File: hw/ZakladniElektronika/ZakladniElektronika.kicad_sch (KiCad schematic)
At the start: 2 parts, among them J10 Conn_01x40, J11 Conn_01x40

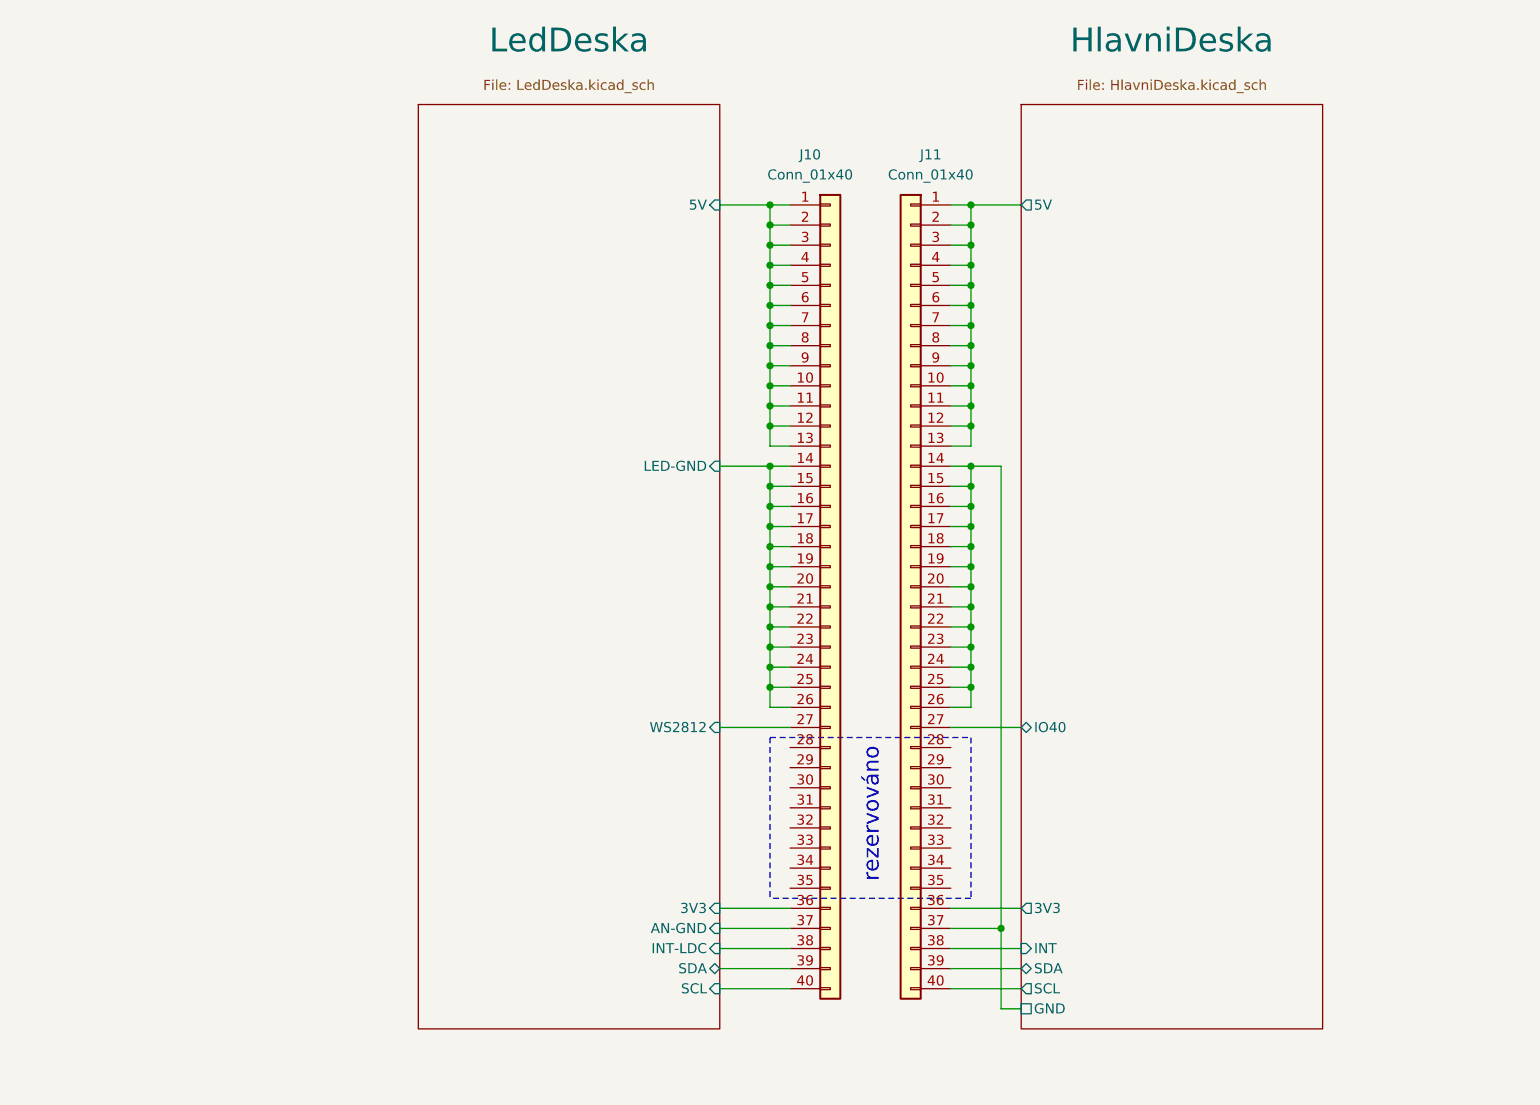
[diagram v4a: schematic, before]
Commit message: Výmněna ochrany baterie
Předchozí ochranný čip JLCPCB nemělo na skladě
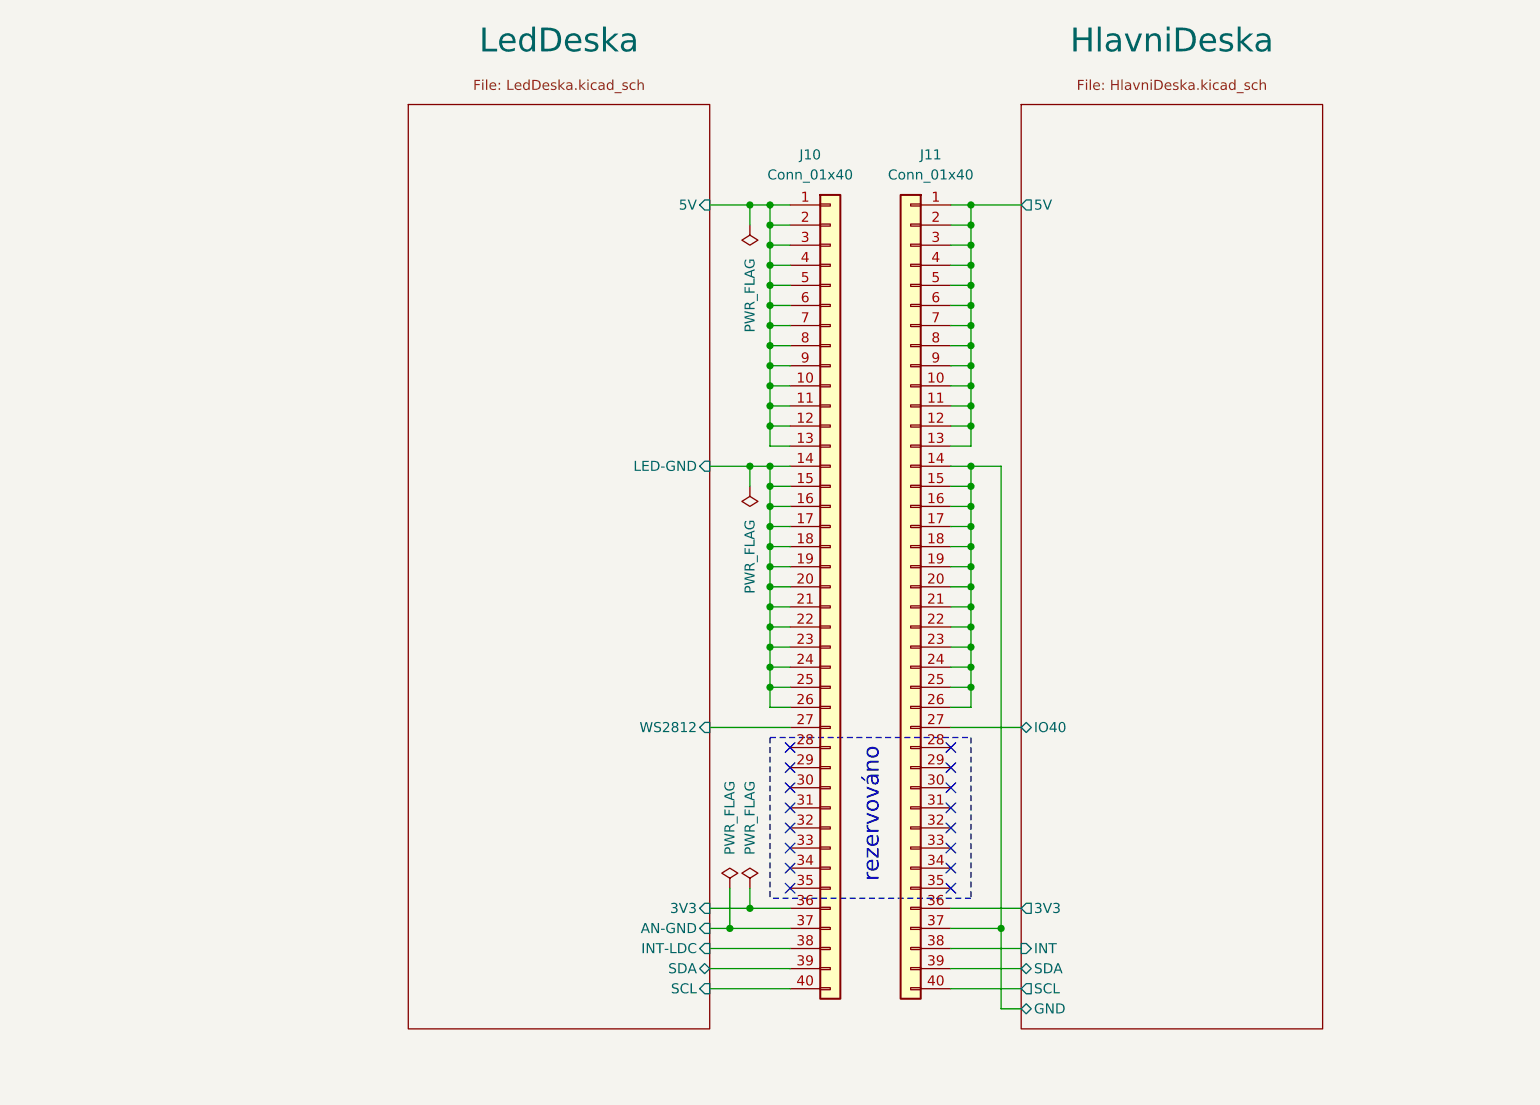
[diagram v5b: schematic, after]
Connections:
- no-connect marks 0 -> 16
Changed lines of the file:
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@@
   (junction (at 146.05 48.26) (diameter 0) (color 0 0 0 0)
   )
+  (junction (at 143.51 134.62) (diameter 0) (color 0 0 0 0)
+  )
   (junction (at 146.05 86.36) (diameter 0) (color 0 0 0 0)
   )
+  (junction (at 140.97 137.16) (diameter 0) (color 0 0 0 0)
+  )
   (junction (at 146.05 106.68) (diameter 0) (color 0 0 0 0)
   )
@@
   (junction (at 146.05 53.34) (diameter 0) (color 0 0 0 0)
   )
+  (junction (at 143.51 45.72) (diameter 0) (color 0 0 0 0)
+  )
   (junction (at 146.05 73.66) (diameter 0) (color 0 0 0 0)
   )
@@
   (junction (at 171.45 71.12) (diameter 0) (color 0 0 0 0)
   )
+  (junction (at 143.51 78.74) (diameter 0) (color 0 0 0 0)
+  )
   (junction (at 146.05 55.88) (diameter 0) (color 0 0 0 0)
   )
@@
   (junction (at 171.45 73.66) (diameter 0) (color 0 0 0 0)
   )
+  (no_connect (at 148.59 127))
+  (no_connect (at 148.59 129.54))
+  (no_connect (at 148.59 116.84))
+  (no_connect (at 168.91 127))
+  (no_connect (at 148.59 119.38))
+  (no_connect (at 148.59 132.08))
+  (no_connect (at 168.91 121.92))
+  (no_connect (at 168.91 116.84))
+  (no_connect (at 168.91 114.3))
+  (no_connect (at 168.91 124.46))
+  (no_connect (at 168.91 132.08))
+  (no_connect (at 168.91 119.38))
+  (no_connect (at 148.59 114.3))
+  (no_connect (at 148.59 121.92))
+  (no_connect (at 148.59 124.46))
+  (no_connect (at 168.91 129.54))
   (wire (pts (xy 177.8 45.72) (xy 171.45 45.72))
     (stroke (width 0) (type default))
@@
     (stroke (width 0) (type default) (color 0 0 0 1))
   )
-  (wire (pts (xy 139.7 134.62) (xy 148.59 134.62))
+  (wire (pts (xy 138.43 134.62) (xy 143.51 134.62))
     (stroke (width 0) (type default))
   )
@@
     (stroke (width 0) (type default) (color 0 0 0 1))
   )
-  (wire (pts (xy 139.7 144.78) (xy 148.59 144.78))
+  (wire (pts (xy 138.43 144.78) (xy 148.59 144.78))
     (stroke (width 0) (type default))
   )
@@
     (stroke (width 0) (type default))
   )
+  (wire (pts (xy 143.51 81.28) (xy 143.51 78.74))
+    (stroke (width 0) (type default))
+  )
   (wire (pts (xy 168.91 142.24) (xy 177.8 142.24))
     (stroke (width 0) (type default))
@@
     (stroke (width 0) (type default))
   )
+  (wire (pts (xy 143.51 45.72) (xy 146.05 45.72))
+    (stroke (width 0) (type default))
+  )
   (wire (pts (xy 168.91 50.8) (xy 171.45 50.8))
     (stroke (width 0) (type default))
@@
     (stroke (width 0) (type default))
   )
+  (wire (pts (xy 143.51 134.62) (xy 148.59 134.62))
+    (stroke (width 0) (type default))
+  )
   (wire (pts (xy 148.59 60.96) (xy 146.05 60.96))
     (stroke (width 0) (type default))
@@
     (stroke (width 0) (type default))
   )
-  (wire (pts (xy 139.7 142.24) (xy 148.59 142.24))
+  (wire (pts (xy 138.43 142.24) (xy 148.59 142.24))
     (stroke (width 0) (type default))
   )
@@
   )
   (wire (pts (xy 148.59 99.06) (xy 146.05 99.06))
+    (stroke (width 0) (type default))
+  )
+  (wire (pts (xy 140.97 132.08) (xy 140.97 137.16))
     (stroke (width 0) (type default))
   )
@@
     (stroke (width 0) (type default))
   )
-  (wire (pts (xy 139.7 137.16) (xy 148.59 137.16))
+  (wire (pts (xy 138.43 137.16) (xy 140.97 137.16))
     (stroke (width 0) (type default))
   )
@@
     (stroke (width 0) (type default))
   )
-  (wire (pts (xy 139.7 111.76) (xy 148.59 111.76))
+  (wire (pts (xy 138.43 111.76) (xy 148.59 111.76))
     (stroke (width 0) (type default))
   )
@@
     (stroke (width 0) (type default) (color 0 0 0 1))
   )
+  (wire (pts (xy 143.51 78.74) (xy 146.05 78.74))
+    (stroke (width 0) (type default))
+  )
   (wire (pts (xy 171.45 86.36) (xy 171.45 83.82))
     (stroke (width 0) (type default) (color 0 0 0 1))
@@
     (stroke (width 0) (type default))
   )
+  (wire (pts (xy 143.51 48.26) (xy 143.51 45.72))
+    (stroke (width 0) (type default))
+  )
   (wire (pts (xy 168.91 83.82) (xy 171.45 83.82))
     (stroke (width 0) (type default) (color 0 0 0 1))
   )
-  (wire (pts (xy 139.7 78.74) (xy 146.05 78.74))
+  (wire (pts (xy 138.43 78.74) (xy 143.51 78.74))
     (stroke (width 0) (type default))
   )
@@
     (stroke (width 0) (type default))
   )
-  (wire (pts (xy 139.7 45.72) (xy 146.05 45.72))
+  (wire (pts (xy 138.43 45.72) (xy 143.51 45.72))
     (stroke (width 0) (type default))
   )
@@
     (stroke (width 0) (type default))
   )
+  (wire (pts (xy 140.97 137.16) (xy 148.59 137.16))
+    (stroke (width 0) (type default))
+  )
   (wire (pts (xy 171.45 63.5) (xy 171.45 60.96))
     (stroke (width 0) (type default))
@@
     (stroke (width 0) (type default))
   )
-  (wire (pts (xy 139.7 139.7) (xy 148.59 139.7))
+  (wire (pts (xy 138.43 139.7) (xy 148.59 139.7))
     (stroke (width 0) (type default))
   )
@@
   )
   (wire (pts (xy 168.91 60.96) (xy 171.45 60.96))
+    (stroke (width 0) (type default))
+  )
+  (wire (pts (xy 143.51 134.62) (xy 143.51 132.08))
     (stroke (width 0) (type default))
   )
@@
     )
   )
+  (symbol (lib_id "power:PWR_FLAG") (at 143.51 132.08 0) (unit 1)
+    (in_bom yes) (on_board yes) (dnp no)
+    (property "Reference" "#FLG05" (at 143.51 130.175 0)
+      (effects (font (size 1.27 1.27)) hide)
+    )
+    (property "Value" "PWR_FLAG" (at 143.51 123.19 90)
+      (effects (font (size 1.27 1.27)))
+    )
+    (property "Footprint" "" (at 143.51 132.08 0)
+      (effects (font (size 1.27 1.27)) hide)
+    )
+    (property "Datasheet" "~" (at 143.51 132.08 0)
+      (effects (font (size 1.27 1.27)) hide)
+    )
+    (pin "1")
+    (instances
+      (project "ZakladniElektronika"
+        (path "/99cd3e15-4eb6-4cbb-8726-789aedd3df15"
+          (reference "#FLG05") (unit 1)
+        )
+      )
+    )
+  )
+  (symbol (lib_id "power:PWR_FLAG") (at 140.97 132.08 0) (unit 1)
+    (in_bom yes) (on_board yes) (dnp no)
+    (property "Reference" "#FLG06" (at 140.97 130.175 0)
+      (effects (font (size 1.27 1.27)) hide)
+    )
+    (property "Value" "PWR_FLAG" (at 140.97 123.19 90)
+      (effects (font (size 1.27 1.27)))
+    )
+    (property "Footprint" "" (at 140.97 132.08 0)
+      (effects (font (size 1.27 1.27)) hide)
+    )
+    (property "Datasheet" "~" (at 140.97 132.08 0)
+      (effects (font (size 1.27 1.27)) hide)
+    )
+    (pin "1")
+    (instances
+      (project "ZakladniElektronika"
+        (path "/99cd3e15-4eb6-4cbb-8726-789aedd3df15"
+          (reference "#FLG06") (unit 1)
+        )
+      )
+    )
+  )
   (symbol (lib_id "Connector_Generic:Conn_01x40") (at 153.67 93.98 0) (unit 1)
     (in_bom yes) (on_board yes) (dnp no)
@@
     )
   )
-  (sheet (at 101.6 33.02) (size 38.1 116.84)
+  (symbol (lib_id "power:PWR_FLAG") (at 143.51 48.26 180) (unit 1)
+    (in_bom yes) (on_board yes) (dnp no)
+    (property "Reference" "#FLG04" (at 143.51 50.165 0)
+      (effects (font (size 1.27 1.27)) hide)
+    )
+    (property "Value" "PWR_FLAG" (at 143.51 57.15 90)
+      (effects (font (size 1.27 1.27)))
+    )
+    (property "Footprint" "" (at 143.51 48.26 0)
+      (effects (font (size 1.27 1.27)) hide)
+    )
+    (property "Datasheet" "~" (at 143.51 48.26 0)
+      (effects (font (size 1.27 1.27)) hide)
+    )
+    (pin "1")
+    (instances
+      (project "ZakladniElektronika"
+        (path "/99cd3e15-4eb6-4cbb-8726-789aedd3df15"
+          (reference "#FLG04") (unit 1)
+        )
+      )
+    )
+  )
+  (symbol (lib_id "power:PWR_FLAG") (at 143.51 81.28 180) (unit 1)
+    (in_bom yes) (on_board yes) (dnp no)
+    (property "Reference" "#FLG02" (at 143.51 83.185 0)
+      (effects (font (size 1.27 1.27)) hide)
+    )
+    (property "Value" "PWR_FLAG" (at 143.51 90.17 90)
+      (effects (font (size 1.27 1.27)))
+    )
+    (property "Footprint" "" (at 143.51 81.28 0)
+      (effects (font (size 1.27 1.27)) hide)
+    )
+    (property "Datasheet" "~" (at 143.51 81.28 0)
+      (effects (font (size 1.27 1.27)) hide)
+    )
+    (pin "1")
+    (instances
+      (project "ZakladniElektronika"
+        (path "/99cd3e15-4eb6-4cbb-8726-789aedd3df15"
+          (reference "#FLG02") (unit 1)
+        )
+      )
+    )
+  )
+  (sheet (at 100.33 33.02) (size 38.1 116.84)
     (stroke (width 0.1524) (type solid))
     (fill (color 0 0 0 0.0000))
-    (property "Sheetname" "LedDeska" (at 120.65 26.67 0)
+    (property "Sheetname" "LedDeska" (at 119.38 26.67 0)
       (effects (font (size 3 3)) (justify bottom))
     )
-    (property "Sheetfile" "LedDeska.kicad_sch" (at 120.65 29.845 0)
+    (property "Sheetfile" "LedDeska.kicad_sch" (at 119.38 29.845 0)
       (effects (font (size 1.27 1.27)) (justify top))
     )
-    (pin "LED-GND" input (at 139.7 78.74 0)
+    (pin "LED-GND" input (at 138.43 78.74 0)
       (effects (font (size 1.27 1.27)) (justify right))
     )
-    (pin "WS2812" input (at 139.7 111.76 0)
+    (pin "WS2812" input (at 138.43 111.76 0)
       (effects (font (size 1.27 1.27)) (justify right))
     )
-    (pin "5V" input (at 139.7 45.72 0)
+    (pin "5V" input (at 138.43 45.72 0)
       (effects (font (size 1.27 1.27)) (justify right))
     )
-    (pin "AN-GND" input (at 139.7 137.16 0)
+    (pin "AN-GND" input (at 138.43 137.16 0)
       (effects (font (size 1.27 1.27)) (justify right))
     )
-    (pin "3V3" input (at 139.7 134.62 0)
+    (pin "3V3" input (at 138.43 134.62 0)
       (effects (font (size 1.27 1.27)) (justify right))
     )
-    (pin "SCL" input (at 139.7 144.78 0)
+    (pin "SCL" input (at 138.43 144.78 0)
       (effects (font (size 1.27 1.27)) (justify right))
     )
-    (pin "SDA" bidirectional (at 139.7 142.24 0)
+    (pin "SDA" bidirectional (at 138.43 142.24 0)
       (effects (font (size 1.27 1.27)) (justify right))
     )
-    (pin "INT-LDC" input (at 139.7 139.7 0)
+    (pin "INT-LDC" input (at 138.43 139.7 0)
       (effects (font (size 1.27 1.27)) (justify right))
     )
@@
       (effects (font (size 1.27 1.27)) (justify left))
     )
-    (pin "GND" passive (at 177.8 147.32 180)
+    (pin "GND" bidirectional (at 177.8 147.32 180)
       (effects (font (size 1.27 1.27)) (justify left))
     )

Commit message: WIP
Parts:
- J10: footprint Connector_FFC-FPC:Molex_52559-3652_2x18-1MP_P0.5mm_Vertical -> RKL-Connectors:AFC11-S40ICC-00
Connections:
- net HlavniDeska/5V renamed HlavniDeska/5V-OUT
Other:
- sheet HlavniDeska ports: added 5V-OUT; removed 5V
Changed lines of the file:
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@@
       (effects (font (size 1.27 1.27)))
     )
-    (property "Footprint" "Connector_FFC-FPC:Molex_52559-3652_2x18-1MP_P0.5mm_Vertical" (at 153.67 93.98 0)
+    (property "Footprint" "RKL-Connectors:AFC11-S40ICC-00" (at 153.67 93.98 0)
       (effects (font (size 1.27 1.27)) hide)
     )
@@
       (effects (font (size 1.27 1.27)) (justify left))
     )
-    (pin "5V" output (at 177.8 45.72 180)
-      (effects (font (size 1.27 1.27)) (justify left))
-    )
     (pin "3V3" output (at 177.8 134.62 180)
       (effects (font (size 1.27 1.27)) (justify left))
@@
       (effects (font (size 1.27 1.27)) (justify left))
     )
+    (pin "5V-OUT" output (at 177.8 45.72 180)
+      (effects (font (size 1.27 1.27)) (justify left))
+    )

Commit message: AHS-V1
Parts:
- added B1: HlavniDeska, RKL-AuxiliarySymbols:Board, symbol RKL-AuxiliarySymbols:Board
- added B2: LedDeska, RKL-AuxiliarySymbols:Board, symbol RKL-AuxiliarySymbols:Board
- J10: JLCPCB_CORRECTION (none) -> 0;0;90
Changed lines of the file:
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@@
       (effects (font (size 1.27 1.27)) hide)
     )
-    (property "Datasheet" "~" (at 163.83 93.98 0)
+    (property "Datasheet" "https://datasheet.lcsc.com/lcsc/2109221430_XUNPU-FPC-05F-40PH20_C2856812.pdf" (at 163.83 93.98 0)
       (effects (font (size 1.27 1.27)) hide)
     )
@@
     )
   )
+  (symbol (lib_id "RKL-AuxiliarySymbols:Board") (at 177.8 33.02 0) (mirror y) (unit 1)
+    (in_bom yes) (on_board yes) (dnp no)
+    (property "Reference" "B1" (at 173.99 33.02 0)
+      (effects (font (size 1.27 1.27)))
+    )
+    (property "Value" "HlavniDeska" (at 170.18 30.48 0)
+      (effects (font (size 1.27 1.27)))
+    )
+    (property "Footprint" "RKL-AuxiliarySymbols:Board" (at 175.26 27.94 0)
+      (effects (font (size 1.27 1.27)) hide)
+    )
+    (property "Datasheet" "" (at 177.8 33.02 0)
+      (effects (font (size 1.27 1.27)) hide)
+    )
+    (instances
+      (project "ZakladniElektronika"
+        (path "/99cd3e15-4eb6-4cbb-8726-789aedd3df15"
+          (reference "B1") (unit 1)
+        )
+      )
+    )
+  )
+  (symbol (lib_id "RKL-AuxiliarySymbols:Board") (at 100.33 33.02 0) (mirror y) (unit 1)
+    (in_bom yes) (on_board yes) (dnp no)
+    (property "Reference" "B2" (at 96.52 33.02 0)
+      (effects (font (size 1.27 1.27)))
+    )
+    (property "Value" "LedDeska" (at 95.25 30.48 0)
+      (effects (font (size 1.27 1.27)))
+    )
+    (property "Footprint" "RKL-AuxiliarySymbols:Board" (at 97.79 27.94 0)
+      (effects (font (size 1.27 1.27)) hide)
+    )
+    (property "Datasheet" "" (at 100.33 33.02 0)
+      (effects (font (size 1.27 1.27)) hide)
+    )
+    (instances
+      (project "ZakladniElektronika"
+        (path "/99cd3e15-4eb6-4cbb-8726-789aedd3df15"
+          (reference "B2") (unit 1)
+        )
+      )
+    )
+  )
   (symbol (lib_id "power:PWR_FLAG") (at 143.51 132.08 0) (unit 1)
     (in_bom yes) (on_board yes) (dnp no)
@@
       (effects (font (size 1.27 1.27)) hide)
     )
-    (property "Datasheet" "~" (at 153.67 93.98 0)
+    (property "Datasheet" "https://datasheet.lcsc.com/lcsc/2212161930_JUSHUO-AFC11-S40ICC-00_C262313.pdf" (at 153.67 93.98 0)
       (effects (font (size 1.27 1.27)) hide)
     )
@@
     )
     (property "Basic/Extended" "E" (at 153.67 93.98 0)
+      (effects (font (size 1.27 1.27)) hide)
+    )
+    (property "JLCPCB_CORRECTION" "0;0;90" (at 153.67 93.98 0)
       (effects (font (size 1.27 1.27)) hide)
     )
@@
     (stroke (width 0.1524) (type solid))
     (fill (color 0 0 0 0.0000))
-    (property "Sheetname" "LedDeska" (at 119.38 26.67 0)
+    (property "Sheetname" "LedDeska" (at 119.38 38.1 0)
       (effects (font (size 3 3)) (justify bottom))
     )
-    (property "Sheetfile" "LedDeska.kicad_sch" (at 119.38 29.845 0)
+    (property "Sheetfile" "LedDeska.kicad_sch" (at 119.38 41.275 0)
       (effects (font (size 1.27 1.27)) (justify top))
     )
@@
     (stroke (width 0.1524) (type solid))
     (fill (color 0 0 0 0.0000))
-    (property "Sheetname" "HlavniDeska" (at 196.85 26.67 0)
+    (property "Sheetname" "HlavniDeska" (at 196.85 38.1 0)
       (effects (font (size 3 3)) (justify bottom))
     )
-    (property "Sheetfile" "HlavniDeska.kicad_sch" (at 196.85 29.845 0)
+    (property "Sheetfile" "HlavniDeska.kicad_sch" (at 196.85 41.275 0)
       (effects (font (size 1.27 1.27)) (justify top))
     )
